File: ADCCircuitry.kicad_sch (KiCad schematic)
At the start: 20 parts, among them U2 ADS112C04, U3 ADS112C04, U4 ADS112C04, U5 ADS112C04

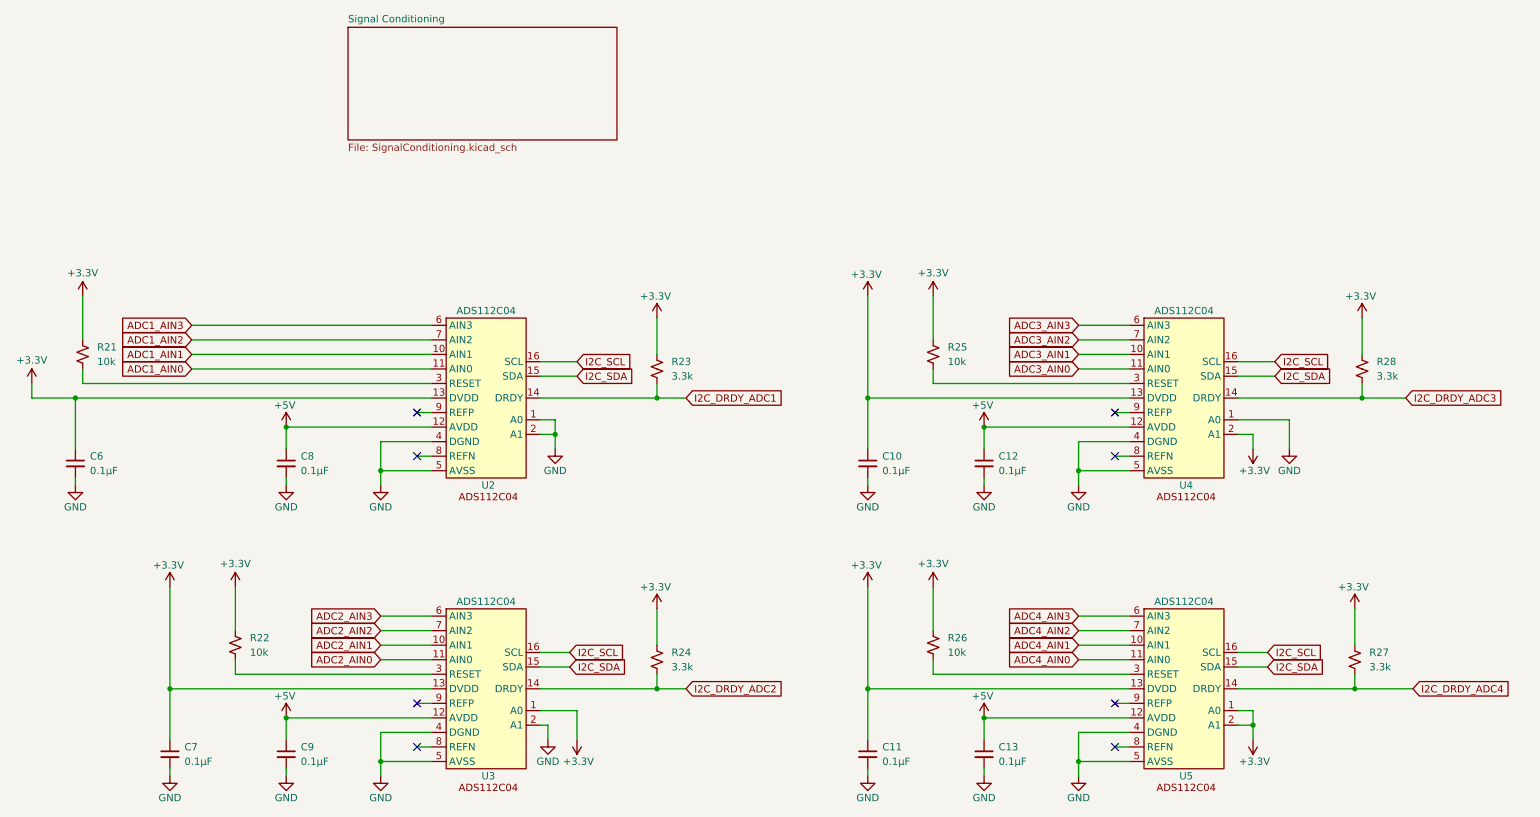
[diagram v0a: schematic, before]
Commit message: revamped schematic to be more readable
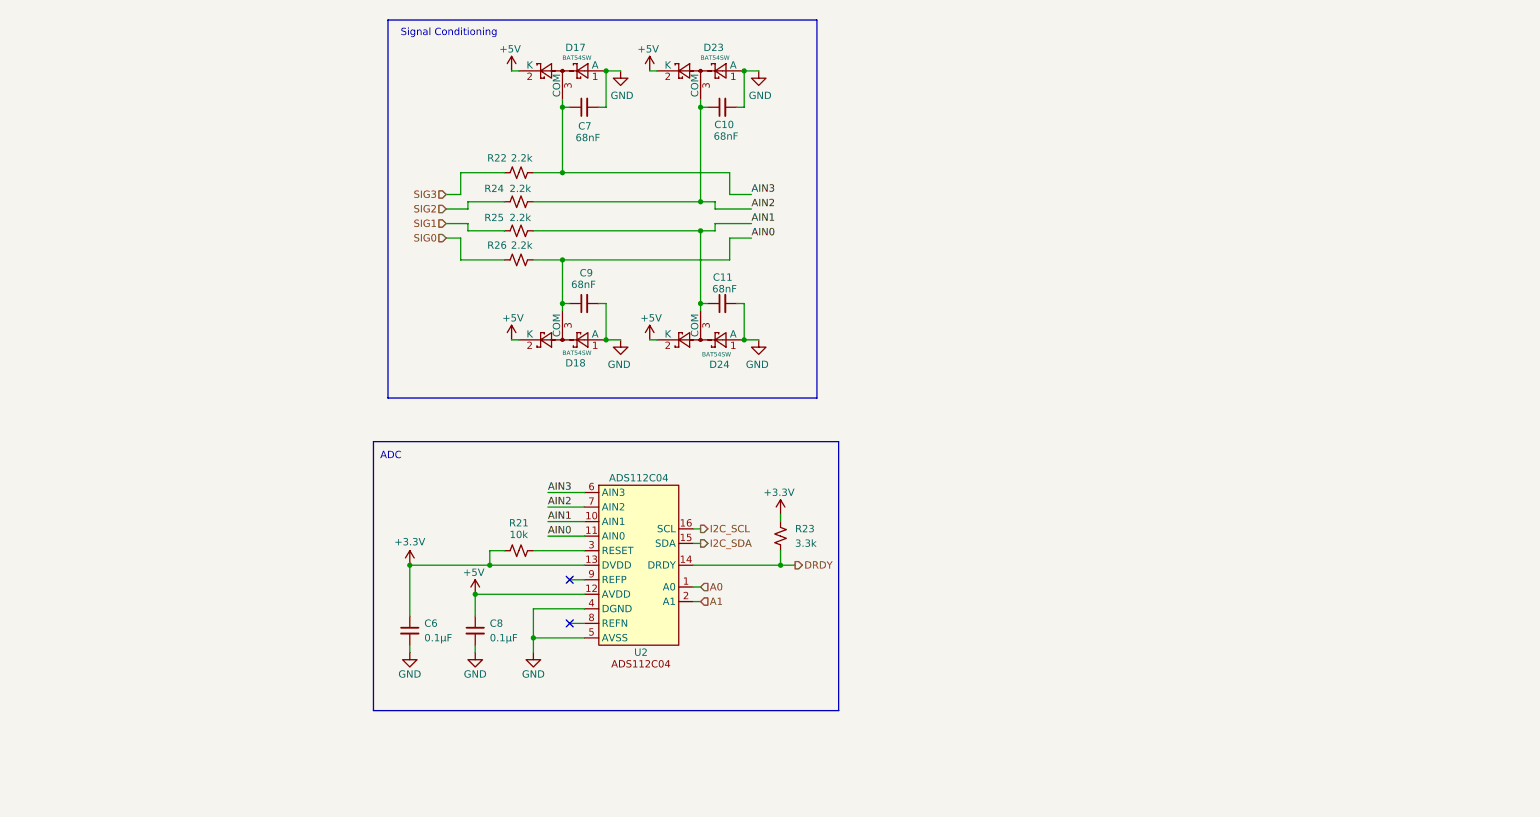
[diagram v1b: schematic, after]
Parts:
- removed C12, C13: 0.1μF, Capacitor_SMD:C_0402_1005Metric, symbol Device:C_Small
- removed R27, R28: 3.3k, Resistor_SMD:R_0402_1005Metric, symbol Device:R_Small_US
- removed U3, U4, U5: ADS112C04, Package_SO:TSSOP-16_4.4x5mm_P0.65mm, symbol ADS112C04:ADS112C04
- added D17, D18, D23, D24: BAT54SW, Package_TO_SOT_SMD:SOT-323_SC-70, symbol Diode:BAT54SW
- C10, C11, C7, C9: value 0.1μF -> 68nF; footprint Capacitor_SMD:C_0402_1005Metric -> Capacitor_SMD:C_0805_2012Metric; LCSC C1525 -> (none); MPN CL05B104KO5NNNC -> (none)
- R22, R25, R26: value 10k -> 2.2k; LCSC C25531 -> (none); MPN 0402WGJ0103TCE -> (none)
- R24: value 3.3k -> 2.2k; LCSC C25890 -> (none); MPN 0402WGF3301TCE -> (none)
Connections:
- net ADC1_AIN0 is gone; now on net AIN0: U2.11 (AIN0)
- net ADC1_AIN1 is gone; now on net AIN1: U2.10 (AIN1)
- net ADC1_AIN3 is gone; now on net AIN3: U2.6 (AIN3)
- net I2C_DRDY_ADC2 is gone; now on net AIN2: R24.2
- net +3.3V: no longer C10.1, C11.1, C7.1, R22.1, R24.1, R25.1, R26.1
- net +5V: now also D17.2 (K), D18.2 (K), D23.2 (K), D24.2 (K); no longer C9.1
- net GND: now also D17.1 (A), D18.1 (A), D23.1 (A), D24.1 (A); no longer U2.1 (A0), U2.2 (A1)
- net AIN1: now reaches R25.2
- net AIN1: now also C11.1, D24.3 (COM)
- net AIN3: now reaches R22.2
- net AIN3: now also C7.1, D17.3 (COM)
- net AIN0: now reaches R26.2
- net AIN0: now also C9.1, D18.3 (COM)
- net ADC1_AIN2 renamed AIN2
- net AIN2: now also C10.1, D23.3 (COM)
- net I2C_DRDY_ADC1 renamed DRDY
- new net A0: U2.1 (A0)
- new net A1: U2.2 (A1)
- new net SIG0: R26.1
- new net SIG1: R25.1
- new net SIG2: R24.1
- new net SIG3: R22.1
- no-connect marks 8 -> 2
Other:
- removed sheet Signal Conditioning
- note added: "ADC"
- note added: "Signal Conditioning"
- moved on the sheet: C6, C8, R21, R23, U2

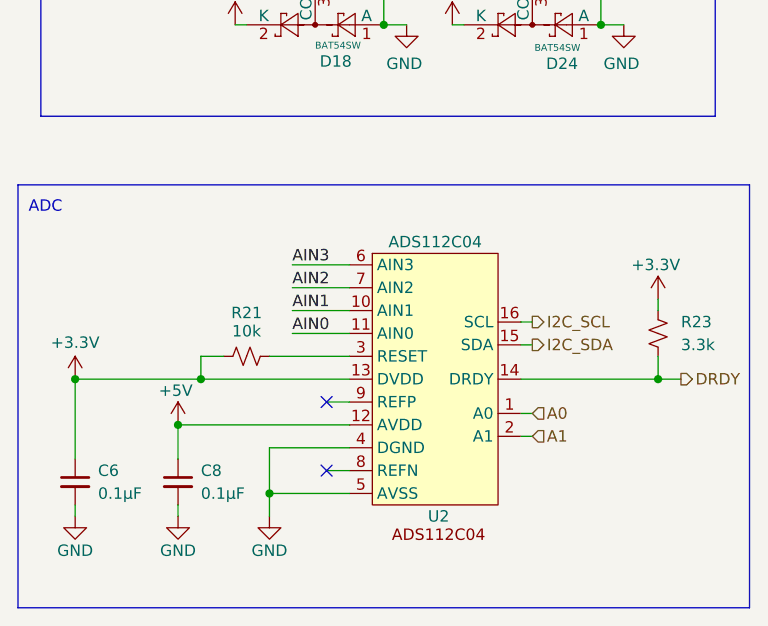
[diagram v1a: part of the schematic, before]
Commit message: add thermocouple filtering, add 5th ADC
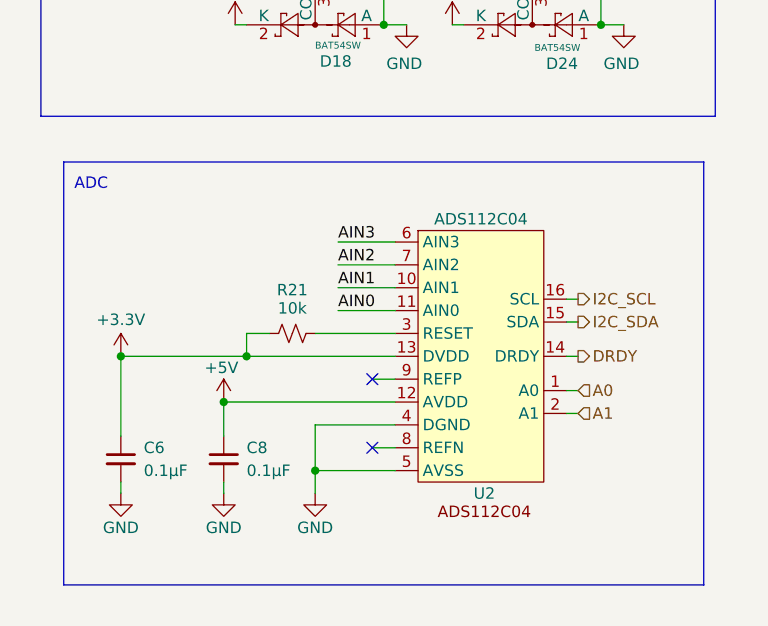
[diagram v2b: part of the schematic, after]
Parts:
- removed R23: 3.3k, Resistor_SMD:R_0402_1005Metric, symbol Device:R_Small_US
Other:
- moved on the sheet: C6, C8, R21, U2

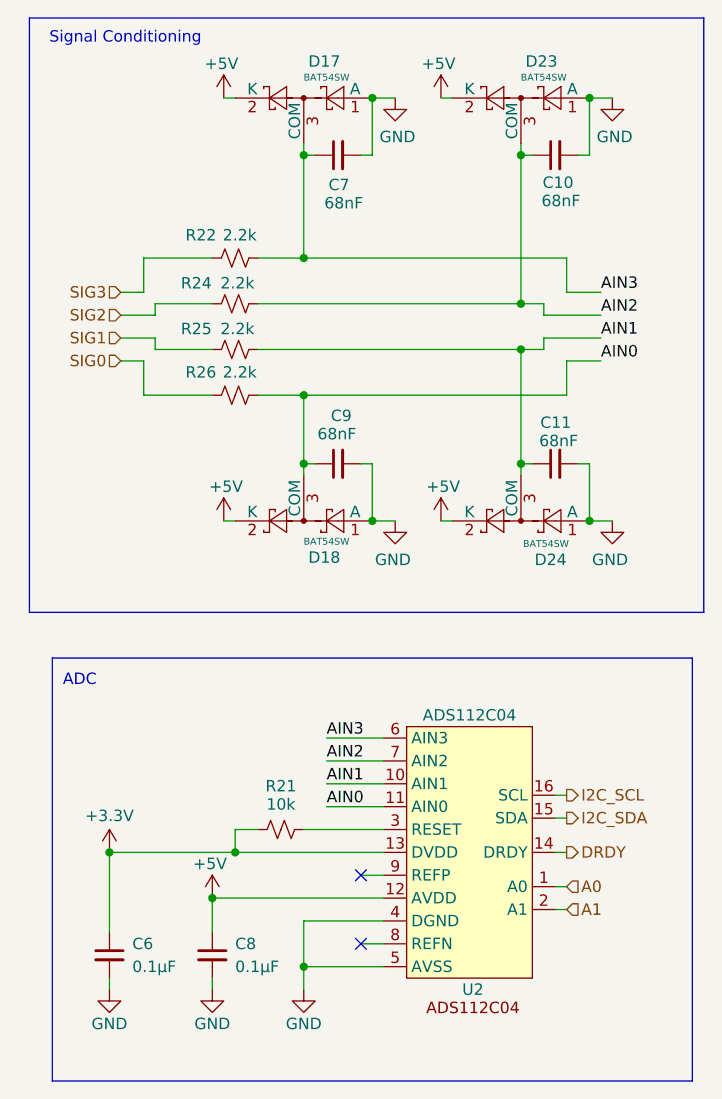
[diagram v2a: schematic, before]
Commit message: add 2 stage lockout to ignitor, add ignitor resistance reading with adc current source
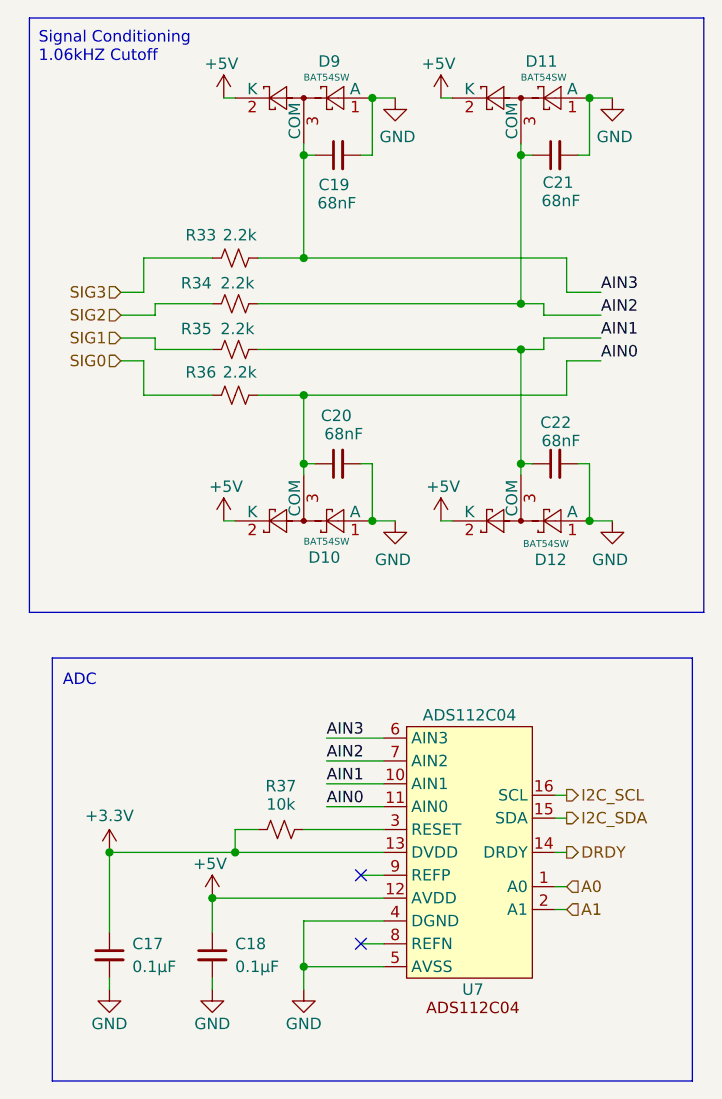
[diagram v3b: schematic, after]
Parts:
- renumbered C6 to C17, C8 to C18, C7 to C19, C9 to C20, C10 to C21, C11 to C22, D18 to D10, D23 to D11, D24 to D12, D17 to D9, R22 to R33, R24 to R34, R25 to R35, R26 to R36, R21 to R37, U2 to U7
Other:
- note added: "Signal Conditioning 1.06kHZ Cutoff"
- note removed: "Signal Conditioning"
